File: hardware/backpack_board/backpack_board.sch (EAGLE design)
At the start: 21 parts, among them Q1 MOSFET-NCHANNEL2N7000

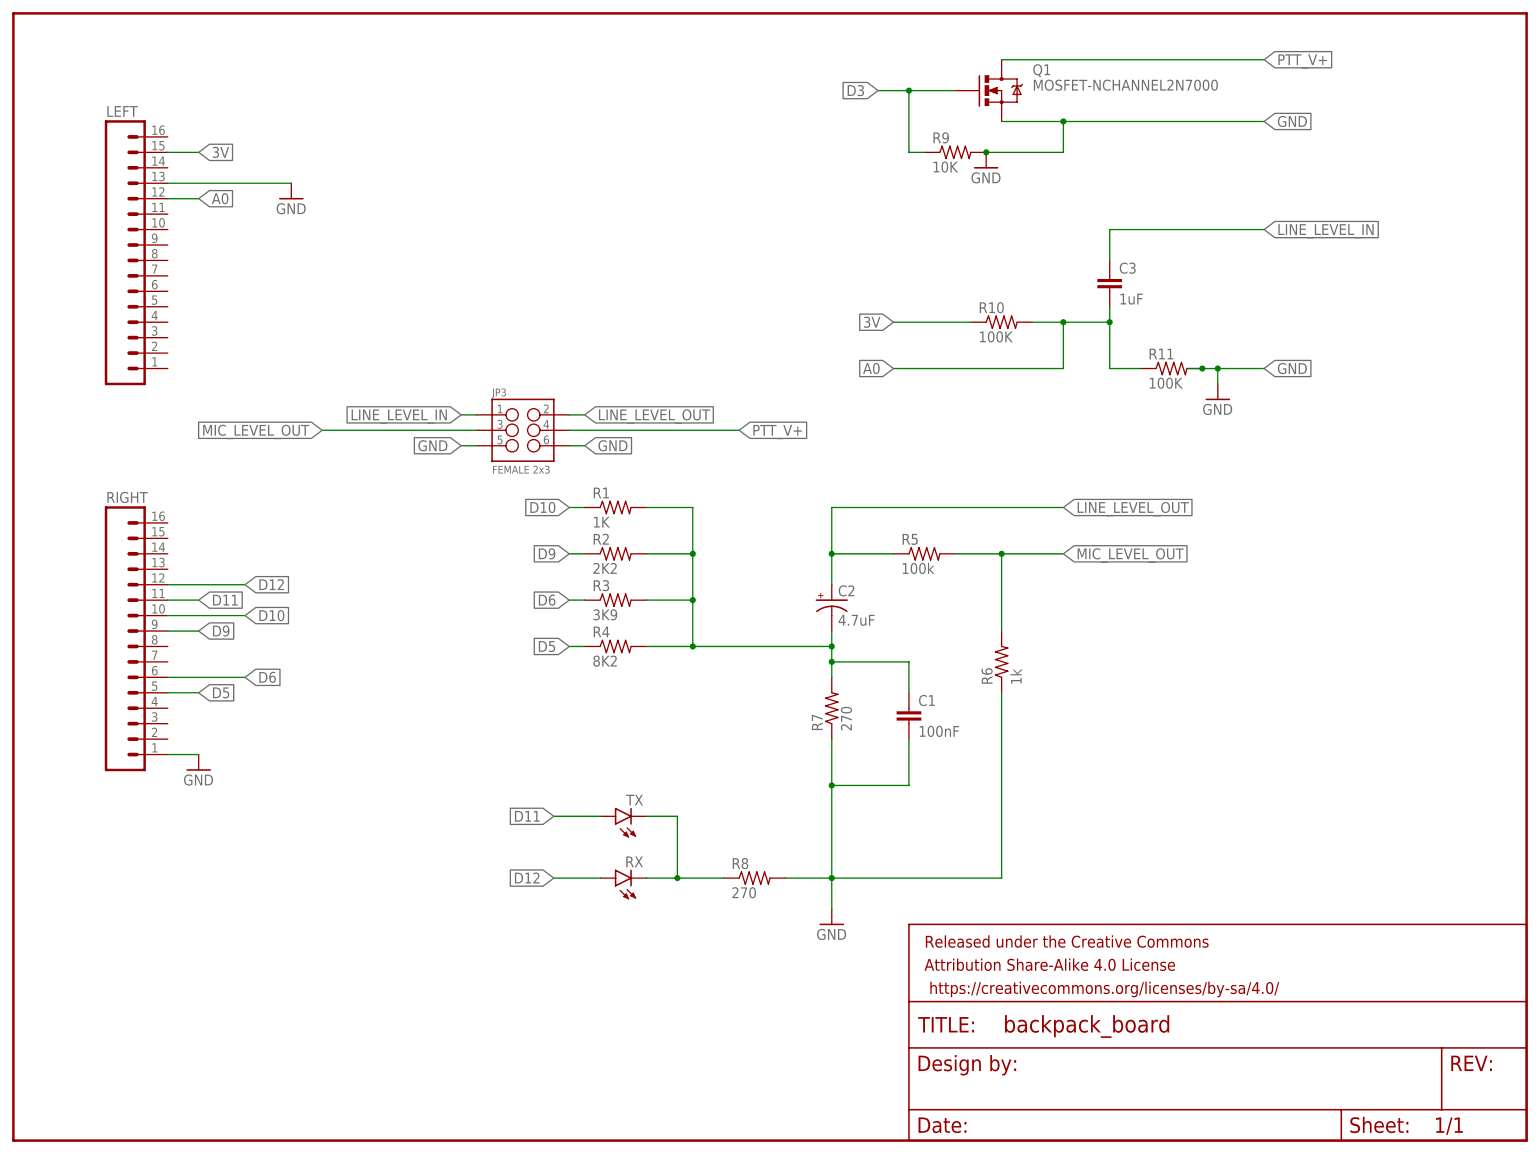
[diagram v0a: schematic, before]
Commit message: add silkscreen and drill holes to design
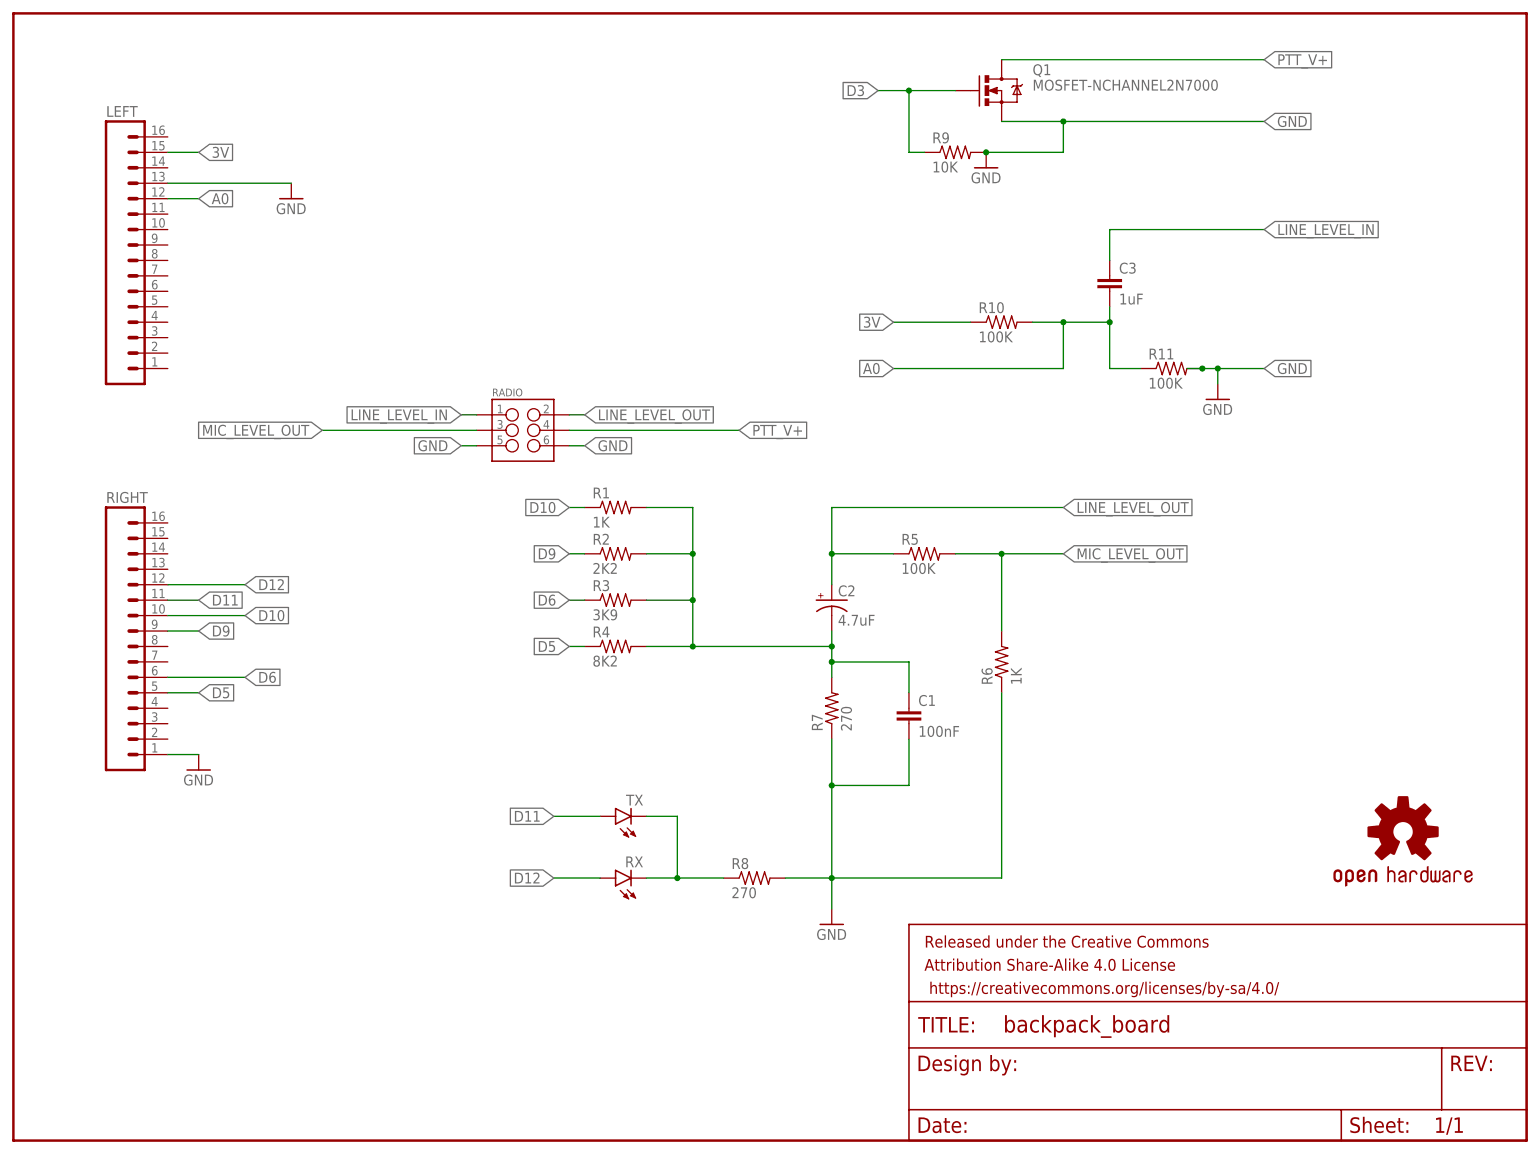
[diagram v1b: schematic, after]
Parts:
- added LOGO1: OSHW-LOGOM, SparkFun-Aesthetics:OSHW-LOGOM
- R5: value 100k -> 100K
- R6: value 1k -> 1K
- RADIO: value FEMALE 2x3 -> (none)
- renumbered JP3 to RADIO
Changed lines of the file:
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@@
 <part name="R3" library="SparkFun-Passives" deviceset="RESISTOR" device="PTH-1/4W" value="3K9"/>
 <part name="R4" library="SparkFun-Passives" deviceset="RESISTOR" device="PTH-1/4W" value="8K2"/>
-<part name="R5" library="SparkFun-Passives" deviceset="RESISTOR" device="PTH-1/4W" value="100k"/>
-<part name="R6" library="SparkFun-Passives" deviceset="RESISTOR" device="PTH-1/4W" value="1k"/>
+<part name="R5" library="SparkFun-Passives" deviceset="RESISTOR" device="PTH-1/4W" value="100K"/>
+<part name="R6" library="SparkFun-Passives" deviceset="RESISTOR" device="PTH-1/4W" value="1K"/>
 <part name="R7" library="SparkFun-Passives" deviceset="RESISTOR" device="PTH-1/4W" value="270"/>
 <part name="GND3" library="SparkFun-Aesthetics" deviceset="GND" device=""/>
@@
 <part name="GND4" library="SparkFun-Aesthetics" deviceset="GND" device=""/>
 <part name="GND5" library="SparkFun-Aesthetics" deviceset="GND" device=""/>
-<part name="JP3" library="SparkFun-Connectors" deviceset="M03X2" device="FEMALE" value="FEMALE 2x3"/>
+<part name="RADIO" library="SparkFun-Connectors" deviceset="M03X2" device="FEMALE"/>
+<part name="LOGO1" library="SparkFun-Aesthetics" deviceset="OSHW-LOGO" device="M"/>
 </parts>
 <sheets>
@@
 </plain>
 <instances>
-<instance part="LEFT" gate="G$1" x="15.24" y="147.32"/>
-<instance part="RIGHT" gate="G$1" x="15.24" y="83.82"/>
+<instance part="LEFT" gate="G$1" x="15.24" y="147.32" smashed="yes">
+<attribute name="VALUE" x="15.24" y="121.92" size="1.778" layer="96"/>
+<attribute name="NAME" x="15.24" y="168.402" size="1.778" layer="95"/>
+</instance>
+<instance part="RIGHT" gate="G$1" x="15.24" y="83.82" smashed="yes">
+<attribute name="VALUE" x="15.24" y="58.42" size="1.778" layer="96"/>
+<attribute name="NAME" x="15.24" y="104.902" size="1.778" layer="95"/>
+</instance>
 <instance part="FRAME1" gate="G$1" x="0" y="0"/>
 <instance part="FRAME1" gate="V" x="147.32" y="0"/>
@@
 <instance part="GND4" gate="1" x="30.48" y="60.96"/>
 <instance part="GND5" gate="1" x="45.72" y="154.94"/>
-<instance part="JP3" gate="G$1" x="83.82" y="116.84"/>
+<instance part="RADIO" gate="G$1" x="83.82" y="116.84" smashed="yes">
+<attribute name="NAME" x="78.74" y="122.428" size="1.27" layer="95"/>
+<attribute name="VALUE" x="78.74" y="109.728" size="1.27" layer="96"/>
+</instance>
+<instance part="LOGO1" gate="G$1" x="228.6" y="50.8"/>
 </instances>
 <busses>
@@
 </segment>
 <segment>
-<pinref part="JP3" gate="G$1" pin="4"/>
+<pinref part="RADIO" gate="G$1" pin="4"/>
 <label x="119.38" y="116.84" size="1.778" layer="95" xref="yes"/>
 <wire x1="91.44" y1="116.84" x2="119.38" y2="116.84" width="0.1524" layer="91"/>
@@
 </segment>
 <segment>
-<pinref part="JP3" gate="G$1" pin="5"/>
+<pinref part="RADIO" gate="G$1" pin="5"/>
 <wire x1="76.2" y1="114.3" x2="73.66" y2="114.3" width="0.1524" layer="91"/>
 <label x="73.66" y="114.3" size="1.778" layer="95" rot="R180" xref="yes"/>
 </segment>
 <segment>
-<pinref part="JP3" gate="G$1" pin="6"/>
+<pinref part="RADIO" gate="G$1" pin="6"/>
 <wire x1="91.44" y1="114.3" x2="93.98" y2="114.3" width="0.1524" layer="91"/>
 <label x="93.98" y="114.3" size="1.778" layer="95" xref="yes"/>
@@
 </segment>
 <segment>
-<pinref part="JP3" gate="G$1" pin="1"/>
+<pinref part="RADIO" gate="G$1" pin="1"/>
 <wire x1="76.2" y1="119.38" x2="73.66" y2="119.38" width="0.1524" layer="91"/>
 <label x="73.66" y="119.38" size="1.778" layer="95" rot="R180" xref="yes"/>
@@
 </segment>
 <segment>
-<pinref part="JP3" gate="G$1" pin="2"/>
+<pinref part="RADIO" gate="G$1" pin="2"/>
 <wire x1="91.44" y1="119.38" x2="93.98" y2="119.38" width="0.1524" layer="91"/>
 <label x="93.98" y="119.38" size="1.778" layer="95" xref="yes"/>
@@
 </segment>
 <segment>
-<pinref part="JP3" gate="G$1" pin="3"/>
+<pinref part="RADIO" gate="G$1" pin="3"/>
 <wire x1="76.2" y1="116.84" x2="50.8" y2="116.84" width="0.1524" layer="91"/>
 <label x="50.8" y="116.84" size="1.778" layer="95" rot="R180" xref="yes"/>

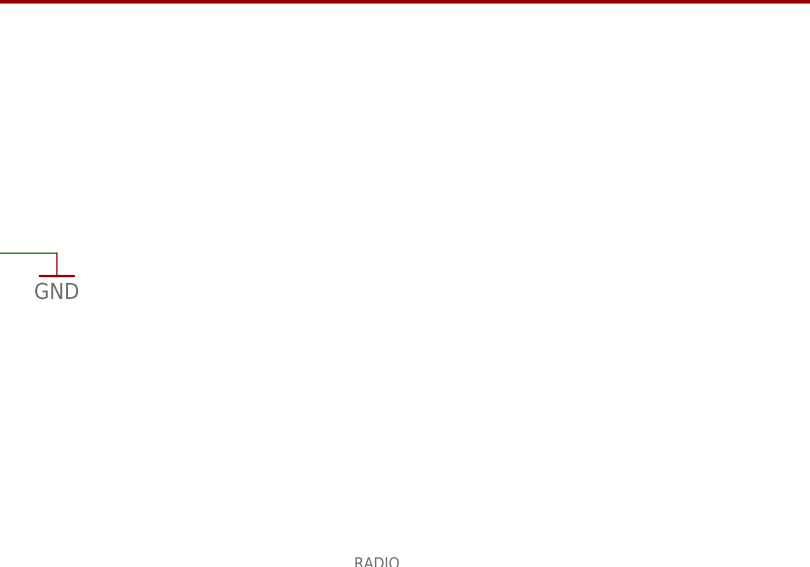
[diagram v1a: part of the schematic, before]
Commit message: add power switch
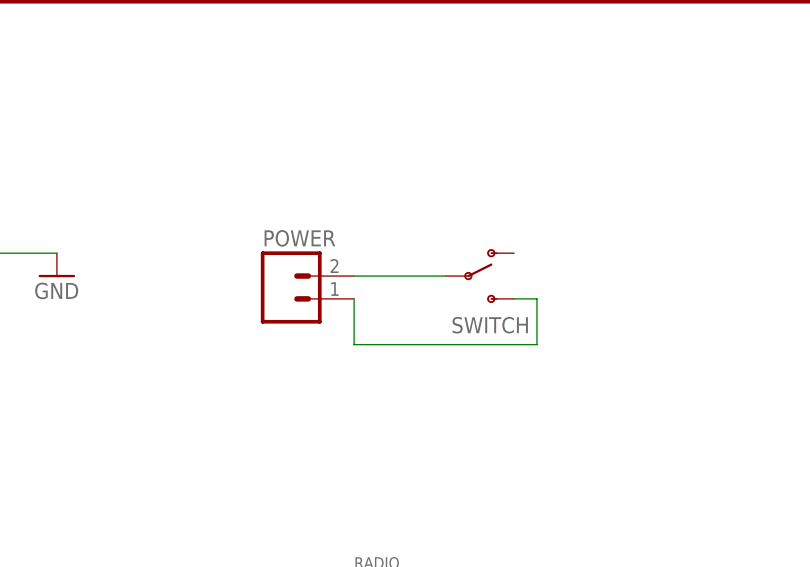
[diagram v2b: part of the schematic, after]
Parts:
- added POWER: (no value), SparkFun-Connectors:M02PTH
- added SWITCH: (no value), SparkFun-Electromechanical:SWITCH-SPDTPTH
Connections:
- new net N$2: POWER.2, SWITCH.P
- new net SWITCH: POWER.1, SWITCH.S
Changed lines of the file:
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@@
 <part name="RADIO" library="SparkFun-Connectors" deviceset="M03X2" device="FEMALE"/>
 <part name="LOGO1" library="SparkFun-Aesthetics" deviceset="OSHW-LOGO" device="M"/>
+<part name="POWER" library="SparkFun-Connectors" deviceset="M02" device="PTH"/>
+<part name="SWITCH" library="SparkFun-Electromechanical" deviceset="SWITCH-SPDT" device="PTH"/>
 </parts>
 <sheets>
@@
 </instance>
 <instance part="LOGO1" gate="G$1" x="228.6" y="50.8"/>
+<instance part="POWER" gate="G$1" x="71.12" y="152.4"/>
+<instance part="SWITCH" gate="1" x="91.44" y="154.94"/>
 </instances>
 <busses>
@@
 </segment>
 </net>
+<net name="N$2" class="0">
+<segment>
+<pinref part="SWITCH" gate="1" pin="P"/>
+<pinref part="POWER" gate="G$1" pin="2"/>
+<wire x1="88.9" y1="154.94" x2="78.74" y2="154.94" width="0.1524" layer="91"/>
+</segment>
+</net>
+<net name="SWITCH" class="0">
+<segment>
+<pinref part="SWITCH" gate="1" pin="S"/>
+<wire x1="96.52" y1="152.4" x2="99.06" y2="152.4" width="0.1524" layer="91"/>
+<wire x1="99.06" y1="152.4" x2="99.06" y2="147.32" width="0.1524" layer="91"/>
+<pinref part="POWER" gate="G$1" pin="1"/>
+<wire x1="99.06" y1="147.32" x2="78.74" y2="147.32" width="0.1524" layer="91"/>
+<wire x1="78.74" y1="147.32" x2="78.74" y2="152.4" width="0.1524" layer="91"/>
+</segment>
+</net>
